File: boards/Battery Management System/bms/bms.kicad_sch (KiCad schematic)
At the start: 5 parts, among them Q1 Q_PMOS_DSG, U1 BD48L32G

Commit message: Schematics
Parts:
- removed C1: uF, symbol Device:C_Small
- removed Q1: Q_PMOS_DSG, symbol Device:Q_PMOS_DSG
- removed R1: 100 kΩ, Resistor_SMD:R_0805_2012Metric, symbol Device:R_Small_US
- added J1: Screw_Terminal_01x05, symbol Connector:Screw_Terminal_01x05
- added J2, J3: Screw_Terminal_01x02, symbol Connector:Screw_Terminal_01x02
- added Q1, Q2, Q3, Q4: PMOS, symbol Simulation_SPICE:PMOS
- added Q5, Q6, Q7, Q8: NMOS, symbol Simulation_SPICE:NMOS
- added R1 (x4): 100kΩ, Resistor_SMD:R_0805_2012Metric, symbol Device:R_Small_US
- added R1 (x3): 5MΩ, Resistor_SMD:R_0805_2012Metric, symbol Device:R_Small_US
- added U2, U3, U4: BD48L32G, Package_TO_SOT_SMD:SOT-23, symbol Power_Management:BD48LxxG
- R1: value ? Ω -> 5MΩ
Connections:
- net GND: now also J1.1 (Pin_1), J2.1 (Pin_1), J3.1 (Pin_1), Q5.3 (S), Q6.3 (S), Q7.3 (S), Q8.3 (S), U2.3 (GND), U3.3 (GND), U4.3 (GND)
- net CON_1: now reaches R1.1, U1.1 (VOUT)
- net CON_1: now also Q5.2 (G)
- net VDD renamed V_CELL_1
- net V_CELL_1: now also J1.5 (Pin_5)
- new net: Q4.2 (G), Q8.1 (D), R1.1
- new net: Q3.3 (S), Q4.1 (D), R1.2
- new net: Q2.2 (G), Q6.1 (D), R1.1
- new net: Q3.2 (G), Q7.1 (D), R1.1
- new net: Q2.3 (S), Q3.1 (D), R1.2
- new net: Q1.2 (G), Q5.1 (D), R1.1
- new net: Q1.3 (S), Q2.1 (D), R1.2
- new net CON_2: Q6.2 (G), R1.1, U2.1 (VOUT)
- new net CON_3: Q7.2 (G), R1.1, U3.1 (VOUT)
- new net CON_4: Q8.2 (G), R1.1, U4.1 (VOUT)
- new net V_BAT_IN: J2.2 (Pin_2), Q1.1 (D), R1.2
- new net V_BAT_OUT: J3.2 (Pin_2), Q4.3 (S)
- new net V_CELL_2: J1.4 (Pin_4), R1.2, U2.2 (VDD)
- new net V_CELL_3: J1.3 (Pin_3), R1.2, U3.2 (VDD)
- new net V_CELL_4: J1.2 (Pin_2), R1.2, U4.2 (VDD)
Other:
- note added: "Battery Charger Input"
- note added: "Battery Input"
- note added: "Battery Output"
- note added: "Prevent Over Discharge"
- note added: "Terminal Blocks"
- note added: "Voltage Detectors"
- moved on the sheet: R1, U1

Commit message: Started PCB layout
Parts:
- J1: footprint (none) -> B5B_XH_A:JST_B5B-XH-A
- J2, J3: footprint (none) -> 1986660_2a:TE_1986660-2
- Q1, Q2, Q3, Q4: footprint (none) -> BSS84_7_F:SOT-23_DIO
- Q5, Q6, Q7, Q8: footprint (none) -> BSS138:SOT95P240X111-3N
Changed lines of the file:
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@@
       (effects (font (size 1.27 1.27)))
     )
-    (property "Footprint" "" (at 38.354 86.868 0)
+    (property "Footprint" "1986660_2a:TE_1986660-2" (at 38.354 86.868 0)
       (effects (font (size 1.27 1.27)) hide)
     )
@@
       (effects (font (size 1.27 1.27)) (justify left))
     )
-    (property "Footprint" "" (at 69.342 137.922 0)
+    (property "Footprint" "BSS138:SOT95P240X111-3N" (at 69.342 137.922 0)
       (effects (font (size 1.27 1.27)) hide)
     )
@@
       (effects (font (size 1.27 1.27)))
     )
-    (property "Footprint" "" (at 38.354 45.466 0)
+    (property "Footprint" "B5B_XH_A:JST_B5B-XH-A" (at 38.354 45.466 0)
       (effects (font (size 1.27 1.27)) hide)
     )
@@
       (effects (font (size 1.27 1.27)) (justify left))
     )
-    (property "Footprint" "" (at 106.172 137.922 0)
+    (property "Footprint" "BSS138:SOT95P240X111-3N" (at 106.172 137.922 0)
       (effects (font (size 1.27 1.27)) hide)
     )
@@
       (effects (font (size 1.27 1.27)))
     )
-    (property "Footprint" "" (at 82.296 115.316 0)
+    (property "Footprint" "BSS84_7_F:SOT-23_DIO" (at 82.296 115.316 0)
       (effects (font (size 1.27 1.27)) hide)
     )
@@
       (effects (font (size 1.27 1.27)) (justify left))
     )
-    (property "Footprint" "" (at 51.054 137.922 0)
+    (property "Footprint" "BSS138:SOT95P240X111-3N" (at 51.054 137.922 0)
       (effects (font (size 1.27 1.27)) hide)
     )
@@
       (effects (font (size 1.27 1.27)) (justify left))
     )
-    (property "Footprint" "" (at 87.376 137.922 0)
+    (property "Footprint" "BSS138:SOT95P240X111-3N" (at 87.376 137.922 0)
       (effects (font (size 1.27 1.27)) hide)
     )
@@
       (effects (font (size 1.27 1.27)))
     )
-    (property "Footprint" "" (at 45.974 115.316 0)
+    (property "Footprint" "BSS84_7_F:SOT-23_DIO" (at 45.974 115.316 0)
       (effects (font (size 1.27 1.27)) hide)
     )
@@
       (effects (font (size 1.27 1.27)))
     )
-    (property "Footprint" "" (at 101.092 115.316 0)
+    (property "Footprint" "BSS84_7_F:SOT-23_DIO" (at 101.092 115.316 0)
       (effects (font (size 1.27 1.27)) hide)
     )
@@
       (effects (font (size 1.27 1.27)))
     )
-    (property "Footprint" "" (at 38.354 68.58 0)
+    (property "Footprint" "1986660_2a:TE_1986660-2" (at 38.354 68.58 0)
       (effects (font (size 1.27 1.27)) hide)
     )
@@
       (effects (font (size 1.27 1.27)))
     )
-    (property "Footprint" "" (at 64.262 115.316 0)
-      (effects (font (size 1.27 1.27)) hide)
-    )
+    (property "Footprint" "BSS84_7_F:SOT-23_DIO" (at 64.262 115.316 0)
+      (effects (font (size 1.27 1.27)) hide)
+    )

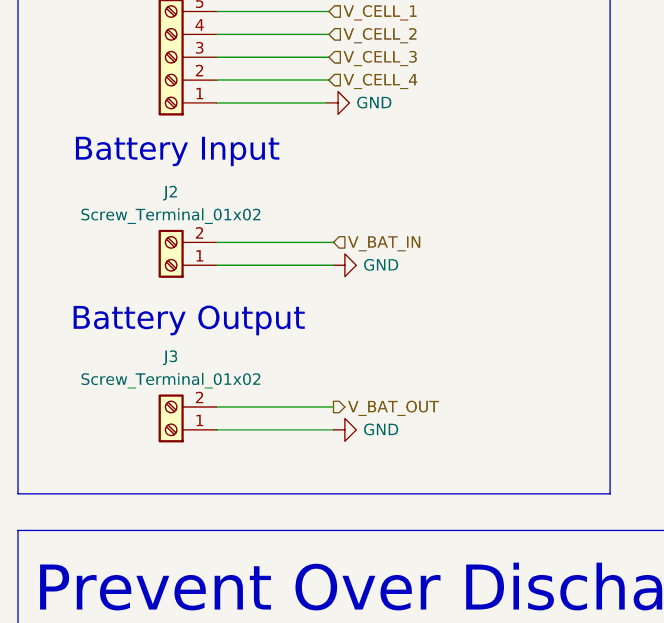
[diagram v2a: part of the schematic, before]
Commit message: updated bms schematic and layout
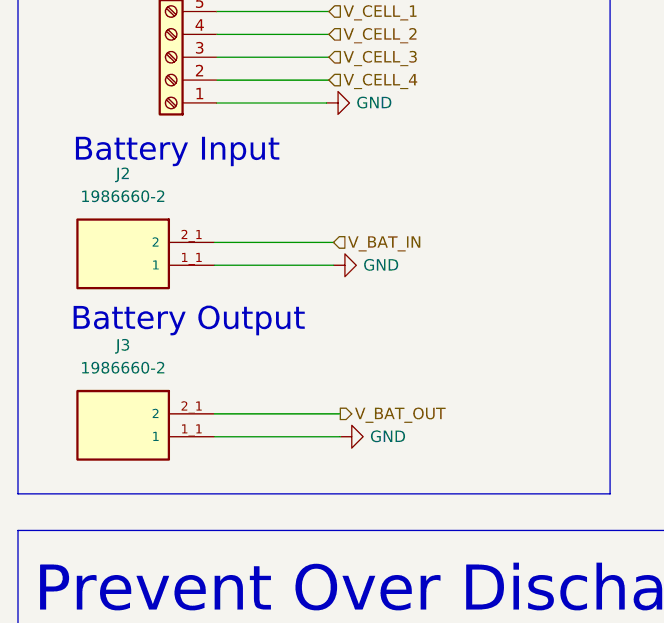
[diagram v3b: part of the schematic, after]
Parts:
- removed J2, J3: Screw_Terminal_01x02, 1986660_2a:TE_1986660-2, symbol Connector:Screw_Terminal_01x02
- added J2, J3: 1986660-2, 1986660_2a:TE_1986660-2, symbol 1986660-2:1986660-2
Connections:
- net GND: now also J2.1_1 (1), J3.1_1 (1)
- net V_BAT_IN: now also J2.2_1 (2)
- net V_BAT_OUT: now also J3.2_1 (2)
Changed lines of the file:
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@@
+    (stroke (width 0) (type default))
+  )
+  (wire (pts (xy 43.18 87.63) (xy 57.15 87.63))
     (stroke (width 0) (type default))
   )
@@
     (stroke (width 0) (type default))
   )
-  (wire (pts (xy 43.434 68.58) (xy 56.388 68.58))
+  (wire (pts (xy 43.18 68.58) (xy 56.388 68.58))
     (stroke (width 0) (type default))
   )
@@
     (stroke (width 0) (type default))
   )
-  (wire (pts (xy 43.434 66.04) (xy 56.388 66.04))
+  (wire (pts (xy 43.18 66.04) (xy 56.388 66.04))
     (stroke (width 0) (type default))
   )
@@
     (stroke (width 0) (type default))
   )
-  (wire (pts (xy 43.434 84.328) (xy 56.388 84.328))
-    (stroke (width 0) (type default))
-  )
   (wire (pts (xy 76.708 126.746) (xy 84.836 126.746))
     (stroke (width 0) (type default))
@@
     (stroke (width 0) (type default))
   )
+  (wire (pts (xy 43.18 85.09) (xy 57.15 85.09))
+    (stroke (width 0) (type default))
+  )
   (wire (pts (xy 43.434 48.006) (xy 55.88 48.006))
     (stroke (width 0) (type default))
   )
   (wire (pts (xy 40.386 126.746) (xy 48.514 126.746))
-    (stroke (width 0) (type default))
-  )
-  (wire (pts (xy 43.434 86.868) (xy 56.388 86.868))
     (stroke (width 0) (type default))
   )
@@
     (effects (font (size 1.27 1.27)) (justify left))
   )
-  (hierarchical_label "V_BAT_OUT" (shape output) (at 56.388 84.328 0) (fields_autoplaced)
+  (hierarchical_label "V_BAT_OUT" (shape output) (at 57.15 85.09 0) (fields_autoplaced)
     (effects (font (size 1.27 1.27)) (justify left))
   )
@@
     )
   )
-  (symbol (lib_id "Connector:Screw_Terminal_01x02") (at 38.354 86.868 180) (unit 1)
-    (in_bom yes) (on_board yes) (dnp no) (fields_autoplaced)
-    (property "Reference" "J3" (at 38.354 78.74 0)
-      (effects (font (size 1.27 1.27)))
-    )
-    (property "Value" "Screw_Terminal_01x02" (at 38.354 81.28 0)
-      (effects (font (size 1.27 1.27)))
-    )
-    (property "Footprint" "1986660_2a:TE_1986660-2" (at 38.354 86.868 0)
-      (effects (font (size 1.27 1.27)) hide)
-    )
-    (property "Datasheet" "~" (at 38.354 86.868 0)
-      (effects (font (size 1.27 1.27)) hide)
-    )
-    (pin "1")
-    (pin "2")
-    (instances
-      (project "bms"
-        (path "/e0ec80f6-0ac5-448e-a052-7eb38c8b1976"
-          (reference "J3") (unit 1)
-        )
-      )
-    )
-  )
   (symbol (lib_id "Simulation_SPICE:NMOS") (at 64.262 140.462 0) (unit 1)
     (in_bom yes) (on_board yes) (dnp no) (fields_autoplaced)
@@
     )
   )
-  (symbol (lib_id "power:GND") (at 56.388 86.868 90) (unit 1)
-    (in_bom yes) (on_board yes) (dnp no) (fields_autoplaced)
-    (property "Reference" "#PWR05" (at 62.738 86.868 0)
-      (effects (font (size 1.27 1.27)) hide)
-    )
-    (property "Value" "GND" (at 59.69 86.868 90)
-      (effects (font (size 1.27 1.27)) (justify right))
-    )
-    (property "Footprint" "" (at 56.388 86.868 0)
-      (effects (font (size 1.27 1.27)) hide)
-    )
-    (property "Datasheet" "" (at 56.388 86.868 0)
+  (symbol (lib_id "power:GND") (at 57.15 87.63 90) (unit 1)
+    (in_bom yes) (on_board yes) (dnp no) (fields_autoplaced)
+    (property "Reference" "#PWR05" (at 63.5 87.63 0)
+      (effects (font (size 1.27 1.27)) hide)
+    )
+    (property "Value" "GND" (at 60.452 87.63 90)
+      (effects (font (size 1.27 1.27)) (justify right))
+    )
+    (property "Footprint" "" (at 57.15 87.63 0)
+      (effects (font (size 1.27 1.27)) hide)
+    )
+    (property "Datasheet" "" (at 57.15 87.63 0)
       (effects (font (size 1.27 1.27)) hide)
     )
@@
     )
   )
+  (symbol (lib_id "1986660-2:1986660-2") (at 33.02 85.09 180) (unit 1)
+    (in_bom yes) (on_board yes) (dnp no) (fields_autoplaced)
+    (property "Reference" "J3" (at 33.02 77.47 0)
+      (effects (font (size 1.27 1.27)))
+    )
+    (property "Value" "1986660-2" (at 33.02 80.01 0)
+      (effects (font (size 1.27 1.27)))
+    )
+    (property "Footprint" "1986660_2a:TE_1986660-2" (at 33.02 85.09 0)
+      (effects (font (size 1.27 1.27)) (justify bottom) hide)
+    )
+    (property "Datasheet" "" (at 33.02 85.09 0)
+      (effects (font (size 1.27 1.27)) hide)
+    )
+    (property "COMMENT" "1986660-2" (at 33.02 85.09 0)
+      (effects (font (size 1.27 1.27)) (justify bottom) hide)
+    )
+    (property "MF" "TE Connectivity" (at 33.02 85.09 0)
+      (effects (font (size 1.27 1.27)) (justify bottom) hide)
+    )
+    (property "DESCRIPTION" "Conn Terminal Block 2 POS 10.16mm Solder ST Thru-Hole 65A Package" (at 33.02 85.09 0)
+      (effects (font (size 1.27 1.27)) (justify bottom) hide)
+    )
+    (property "PACKAGE" "None" (at 33.02 85.09 0)
+      (effects (font (size 1.27 1.27)) (justify bottom) hide)
+    )
+    (property "PRICE" "None" (at 33.02 85.09 0)
+      (effects (font (size 1.27 1.27)) (justify bottom) hide)
+    )
+    (property "TE_PURCHASE_URL" "https://www.te.com/usa-en/product-1986660-2.html?te_bu=Cor&te_type=disp&te_campaign=seda_glo_cor-seda-global-disp-prtnr-fy19-seda-model-bom-cta_sma-317_1&elqCampaignId=32493" (at 33.02 85.09 0)
+      (effects (font (size 1.27 1.27)) (justify bottom) hide)
+    )
+    (property "MP" "1986660-2" (at 33.02 85.09 0)
+      (effects (font (size 1.27 1.27)) (justify bottom) hide)
+    )
+    (property "AVAILABILITY" "Unavailable" (at 33.02 85.09 0)
+      (effects (font (size 1.27 1.27)) (justify bottom) hide)
+    )
+    (pin "1_1")
+    (pin "2_1")
+    (instances
+      (project "bms"
+        (path "/e0ec80f6-0ac5-448e-a052-7eb38c8b1976"
+          (reference "J3") (unit 1)
+        )
+      )
+    )
+  )
   (symbol (lib_id "power:GND") (at 164.338 44.196 270) (unit 1)
     (in_bom yes) (on_board yes) (dnp no)
@@
     )
   )
-  (symbol (lib_id "Connector:Screw_Terminal_01x02") (at 38.354 68.58 180) (unit 1)
-    (in_bom yes) (on_board yes) (dnp no) (fields_autoplaced)
-    (property "Reference" "J2" (at 38.354 60.452 0)
-      (effects (font (size 1.27 1.27)))
-    )
-    (property "Value" "Screw_Terminal_01x02" (at 38.354 62.992 0)
-      (effects (font (size 1.27 1.27)))
-    )
-    (property "Footprint" "1986660_2a:TE_1986660-2" (at 38.354 68.58 0)
-      (effects (font (size 1.27 1.27)) hide)
-    )
-    (property "Datasheet" "~" (at 38.354 68.58 0)
-      (effects (font (size 1.27 1.27)) hide)
-    )
-    (pin "1")
-    (pin "2")
-    (instances
-      (project "bms"
+  (symbol (lib_id "1986660-2:1986660-2") (at 33.02 66.04 180) (unit 1)
+    (in_bom yes) (on_board yes) (dnp no) (fields_autoplaced)
+    (property "Reference" "J2" (at 33.02 58.42 0)
+      (effects (font (size 1.27 1.27)))
+    )
+    (property "Value" "1986660-2" (at 33.02 60.96 0)
+      (effects (font (size 1.27 1.27)))
+    )
+    (property "Footprint" "1986660_2a:TE_1986660-2" (at 33.02 66.04 0)
+      (effects (font (size 1.27 1.27)) (justify bottom) hide)
+    )
+    (property "Datasheet" "" (at 33.02 66.04 0)
+      (effects (font (size 1.27 1.27)) hide)
+    )
+    (property "COMMENT" "1986660-2" (at 33.02 66.04 0)
+      (effects (font (size 1.27 1.27)) (justify bottom) hide)
+    )
+    (property "MF" "TE Connectivity" (at 33.02 66.04 0)
+      (effects (font (size 1.27 1.27)) (justify bottom) hide)
+    )
+    (property "DESCRIPTION" "Conn Terminal Block 2 POS 10.16mm Solder ST Thru-Hole 65A Package" (at 33.02 66.04 0)
+      (effects (font (size 1.27 1.27)) (justify bottom) hide)
+    )
+    (property "PACKAGE" "None" (at 33.02 66.04 0)
+      (effects (font (size 1.27 1.27)) (justify bottom) hide)
+    )
+    (property "PRICE" "None" (at 33.02 66.04 0)
+      (effects (font (size 1.27 1.27)) (justify bottom) hide)
+    )
+    (property "TE_PURCHASE_URL" "https://www.te.com/usa-en/product-1986660-2.html?te_bu=Cor&te_type=disp&te_campaign=seda_glo_cor-seda-global-disp-prtnr-fy19-seda-model-bom-cta_sma-317_1&elqCampaignId=32493" (at 33.02 66.04 0)
+      (effects (font (size 1.27 1.27)) (justify bottom) hide)
+    )
+    (property "MP" "1986660-2" (at 33.02 66.04 0)
+      (effects (font (size 1.27 1.27)) (justify bottom) hide)
+    )
+    (property "AVAILABILITY" "Unavailable" (at 33.02 66.04 0)
+      (effects (font (size 1.27 1.27)) (justify bottom) hide)
+    )
+    (pin "1_1")
+    (pin "2_1")
+    (instances
+      (project "bms"

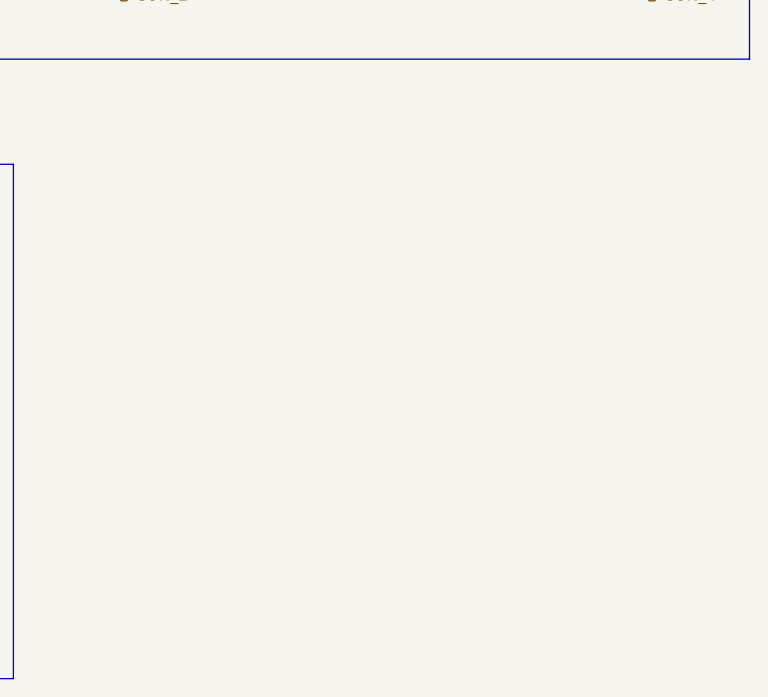
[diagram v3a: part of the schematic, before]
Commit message: Redid pcb layout and added LEDs.
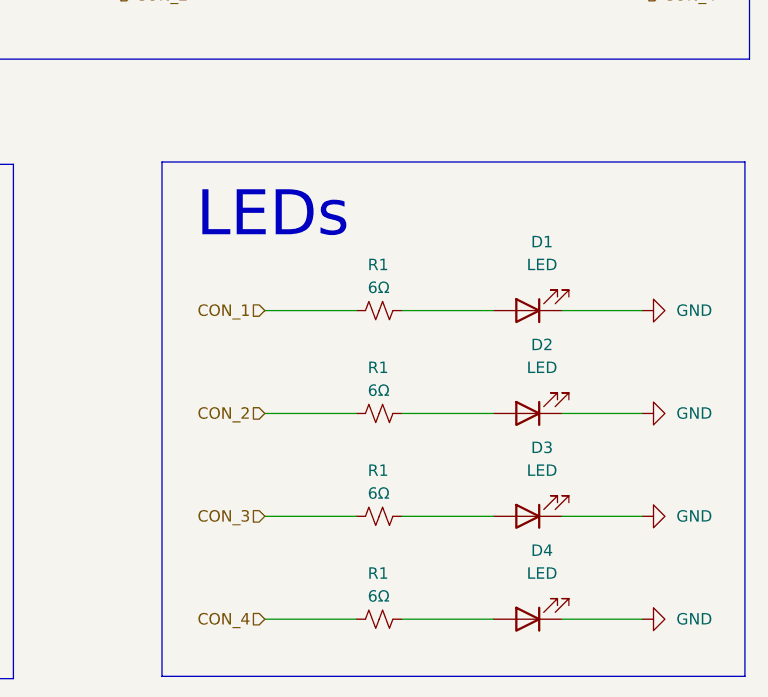
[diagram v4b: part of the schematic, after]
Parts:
- added D1, D2, D3, D4: LED, LED_SMD:LED_0805_2012Metric, symbol Device:LED
- added R1 (x4): 6Ω, Resistor_SMD:R_0805_2012Metric, symbol Device:R_Small_US
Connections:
- net CON_1: now also R1.1
- net CON_2: now also R1.1
- net CON_3: now also R1.1
- net CON_4: now also R1.1
- net GND: now also D1.1 (K), D2.1 (K), D3.1 (K), D4.1 (K)
- new net: D4.2 (A), R1.2
- new net: D2.2 (A), R1.2
- new net: D3.2 (A), R1.2
- new net: D1.2 (A), R1.2
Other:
- note added: "LEDs"
